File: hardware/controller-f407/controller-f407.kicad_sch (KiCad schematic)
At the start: 0 parts

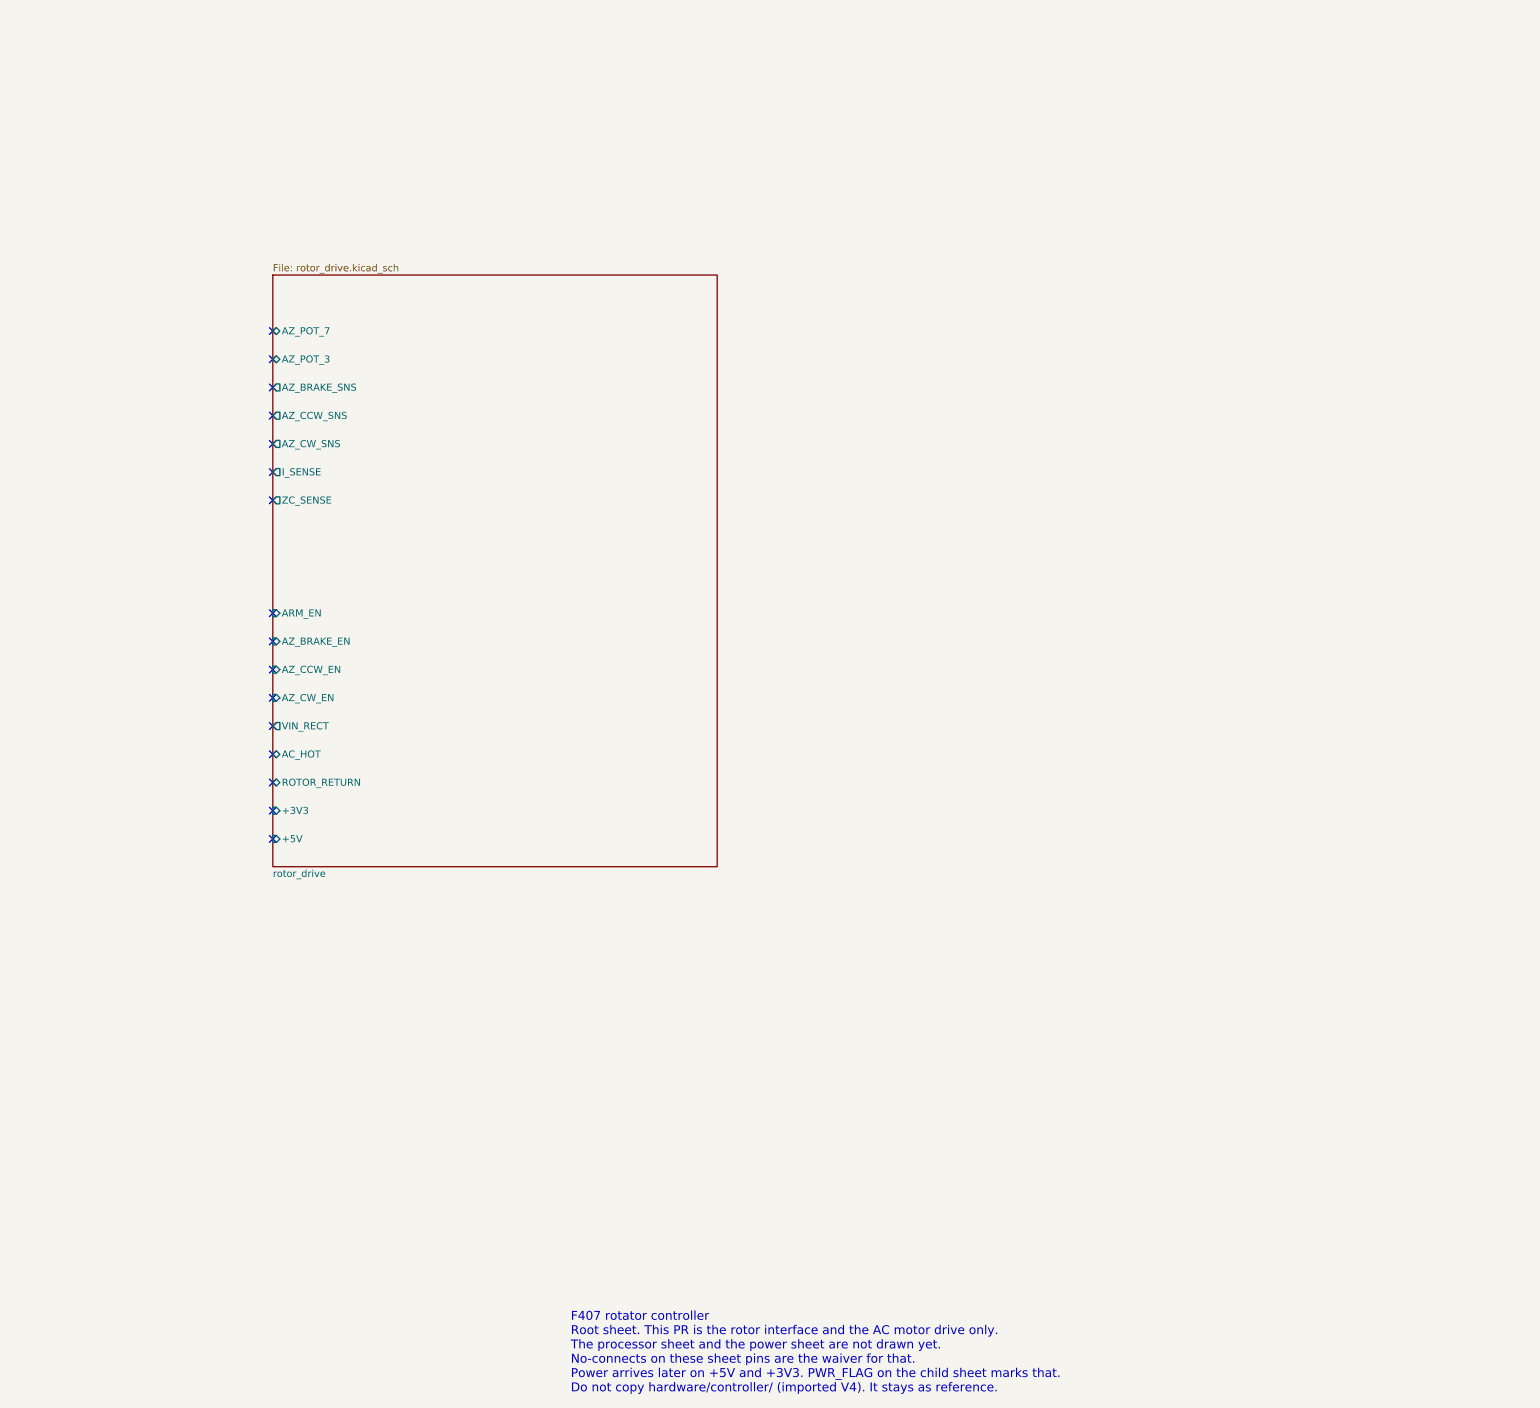
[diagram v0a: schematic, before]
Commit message: Add the Drive MCU and analog sheets, and tidy the triac page.
Tie the dangling ROTOR_RETURN label to GNDPWR, clear overlapping field
text without moving owner-placed parts, and hang drive_mcu and
analog_input off the root. Pin assignment follows ADR 0021.

Co-authored-by: Jeffrey Millar <wa1hco@users.noreply.github.com>
Co-authored-by: Cursor Agent <cursoragent@cursor.com>
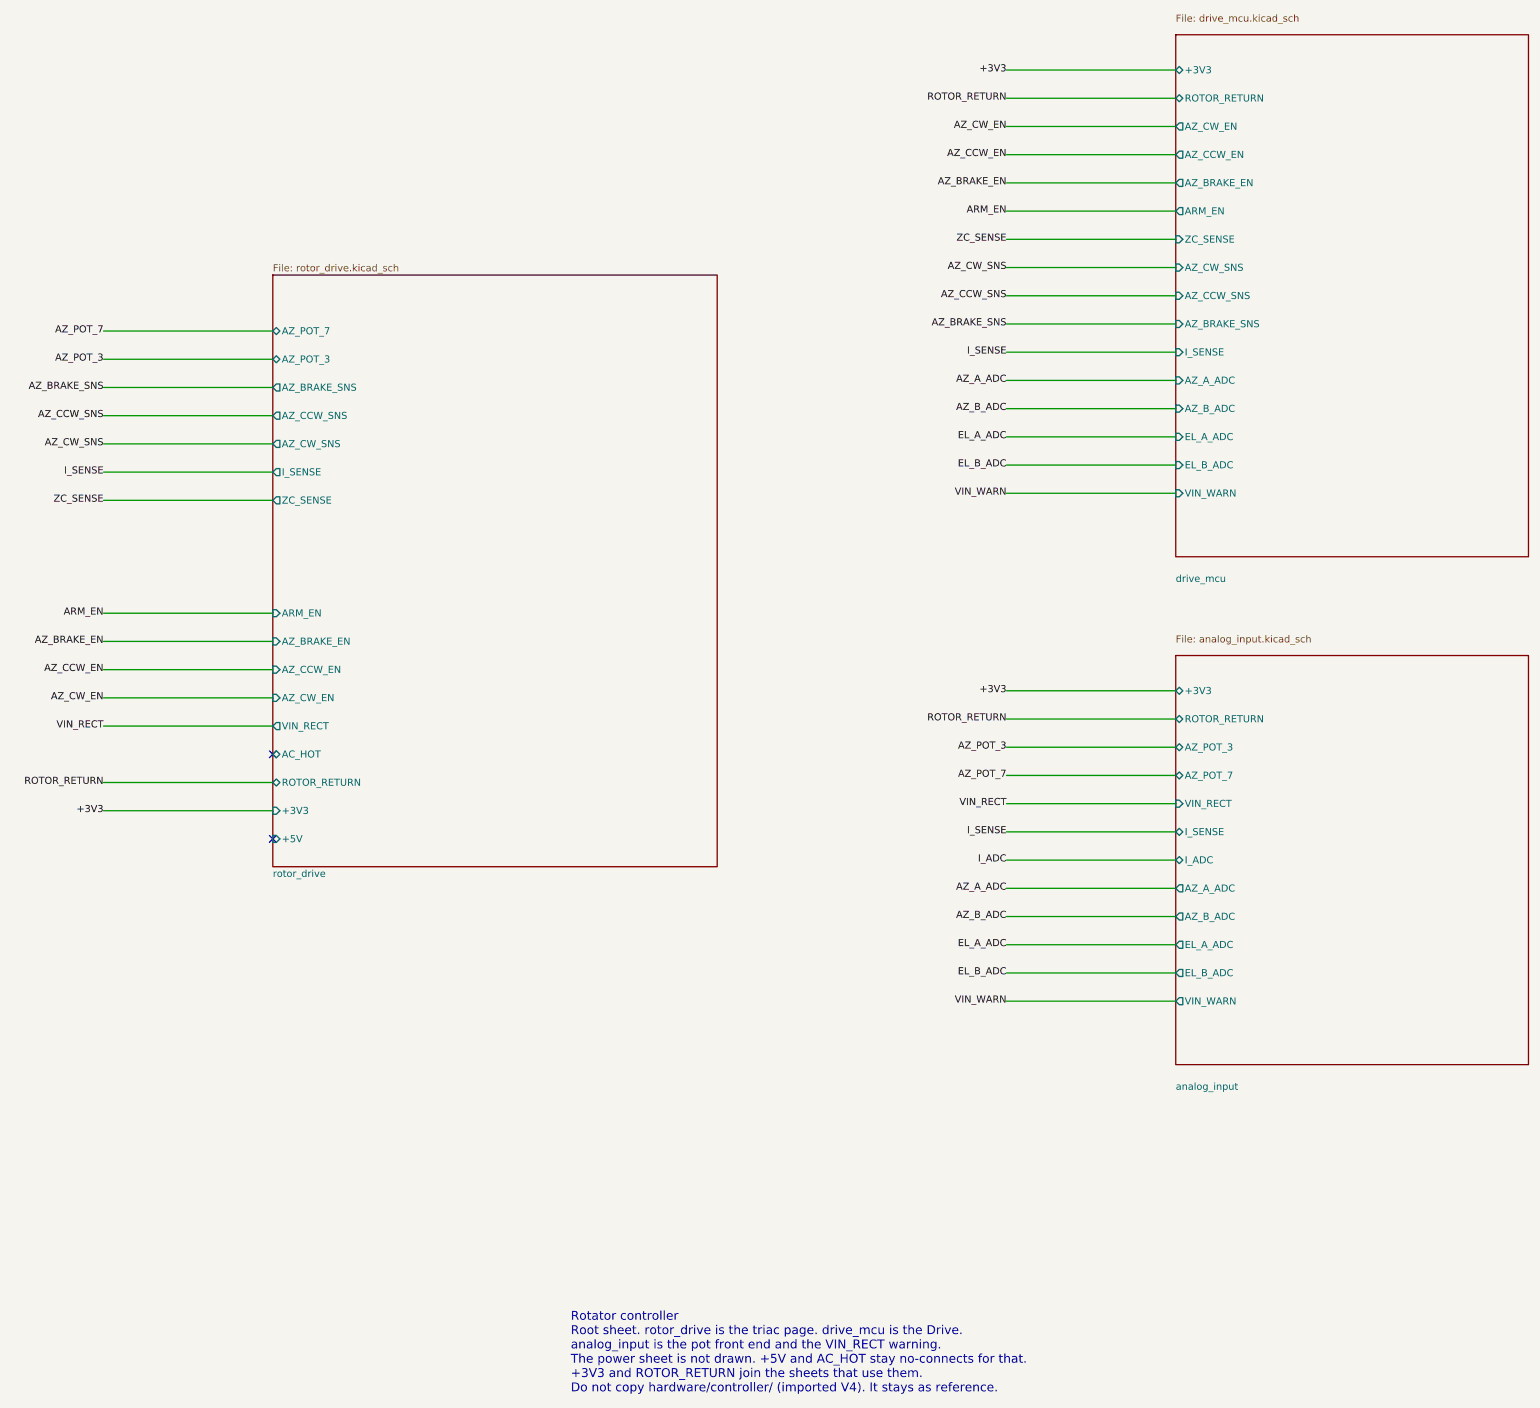
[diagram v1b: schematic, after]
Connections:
- no-connect marks 16 -> 2
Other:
- added sheet analog_input (analog_input.kicad_sch)
- added sheet drive_mcu (drive_mcu.kicad_sch)
- note added: "Rotator controller Root sheet. rotor_drive is the triac page. drive_mcu is the Drive. analog_input is the pot front end and the VIN_RECT warning. The power sheet is not drawn. +5V and AC_HOT stay no-connects for that. +3V3 and ROTOR_RETURN join the sheets that use them. Do not copy hardware/controller/ (imported V4). It stays as reference."
- note removed: "F407 rotator controller Root sheet. This PR is the rotor interface and the AC motor drive only. The processor sheet and the power sheet are not drawn yet. No-connects on these sheet pins are the waiver for that. Power arrives later on +5V and +3V3. PWR_FLAG on the child sheet marks that. Do not copy hardware/controller/ (imported V4). It stays as reference."
